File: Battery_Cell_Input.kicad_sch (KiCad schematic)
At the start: 36 parts, among them J801 Battery_1, J802 HEATER_CONN, J803 HEATER_CONN, Q801 NMOS, Q802 NMOS, U801 BQ76920PW

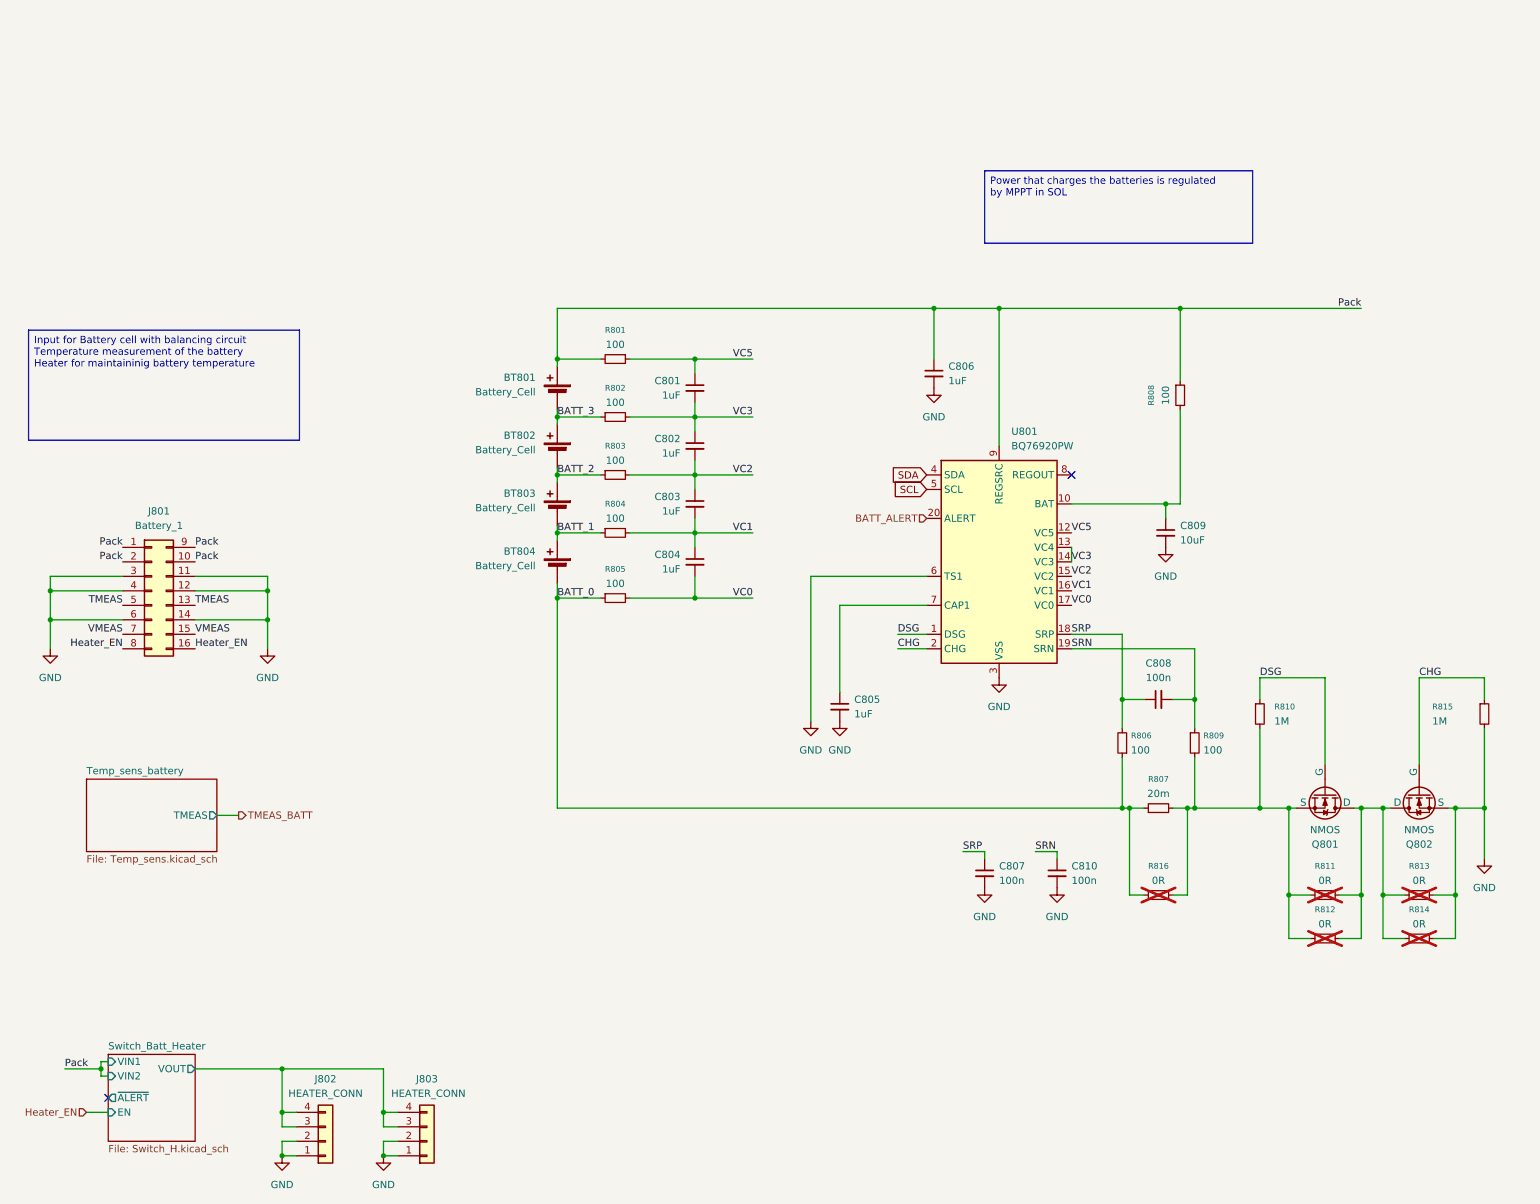
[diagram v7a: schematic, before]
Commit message: wired channel alerts; added schematic for test pbc
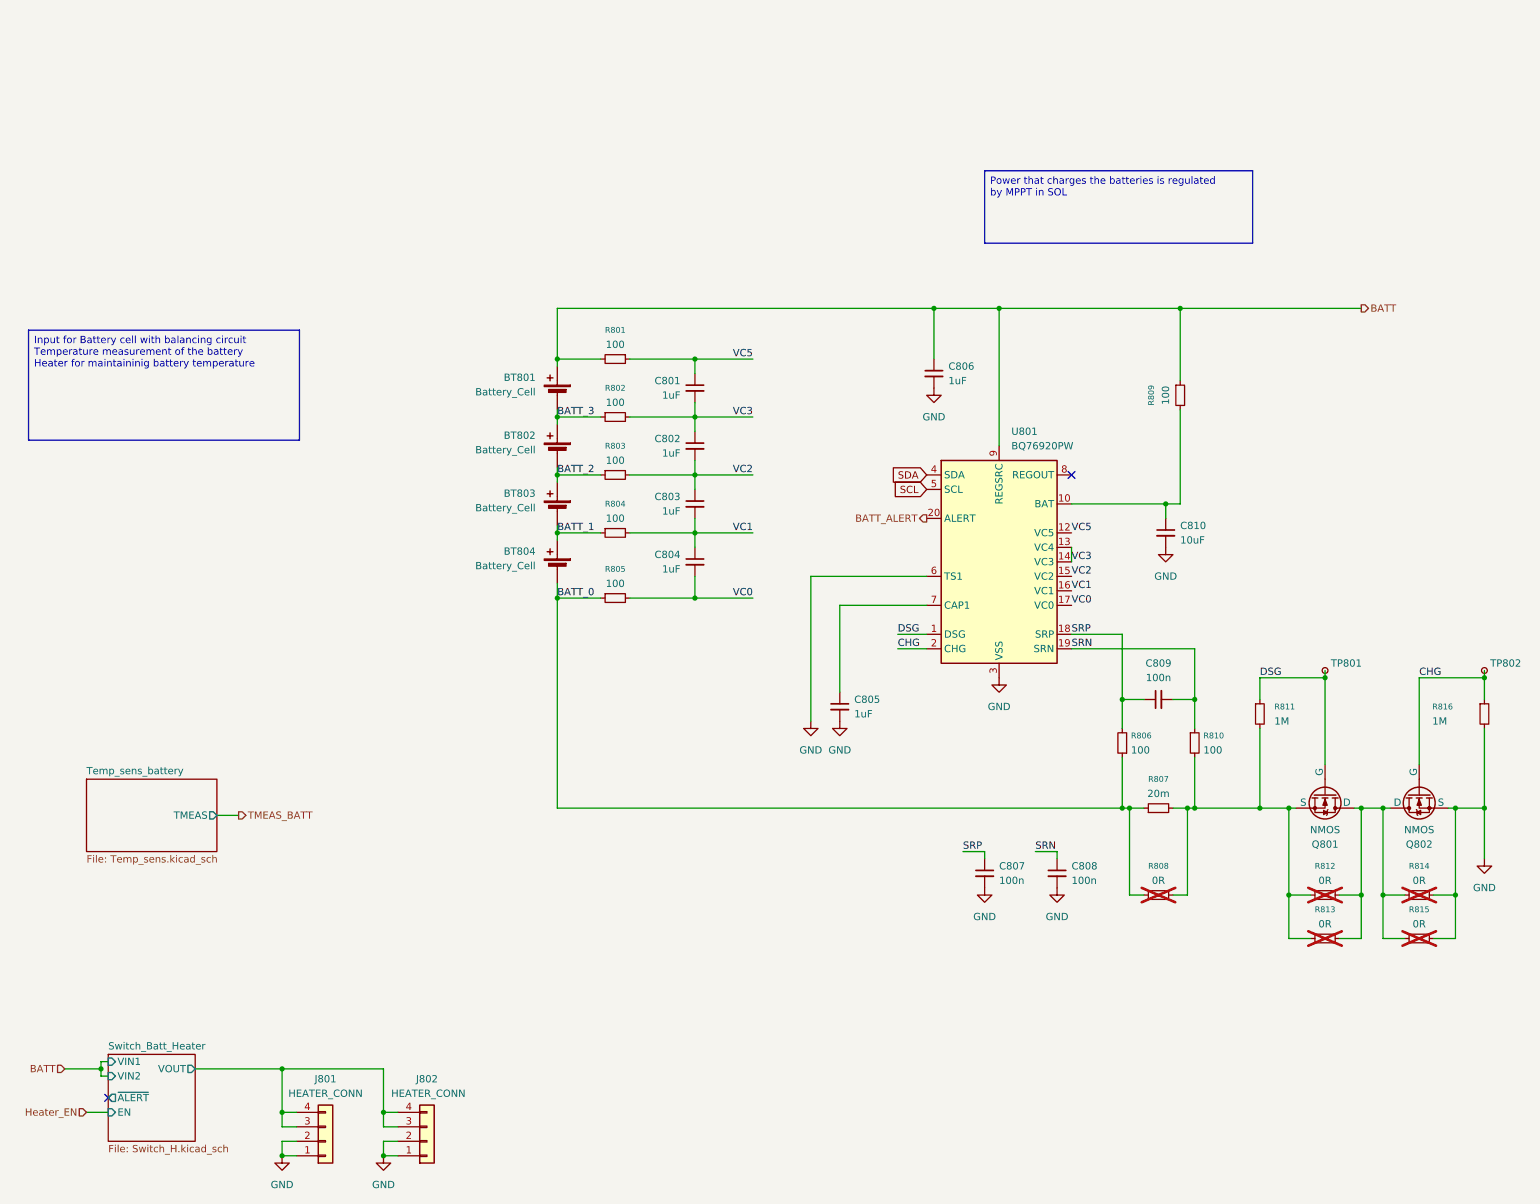
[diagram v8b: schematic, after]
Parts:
- removed J801: Battery_1, Connector_Harwin:Harwin_Gecko-G125-FVX1605L0X_2x08_P1.25mm_Vertical, symbol Connector_Generic:Conn_02x08_Top_Bottom
- added TP801, TP802: ~, TestPoint:TestPoint_Pad_1.0x1.0mm, symbol Connector:TestPoint_Small
- renumbered C810 to C808, C808 to C809, C809 to C810, J802 to J801, J803 to J802, R816 to R808, R808 to R809, R809 to R810, R810 to R811, R811 to R812, R812 to R813, R813 to R814, R814 to R815, R815 to R816
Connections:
- net CHG: now also TP802.1
- net DSG: now also TP801.1
- net Pack renamed BATT
